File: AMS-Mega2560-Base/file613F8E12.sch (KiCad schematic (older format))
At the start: 8 parts, among them IC3 MAX31865AAP+, J2 Conn_01x02, J3 Conn_01x03, J4 Conn_01x02

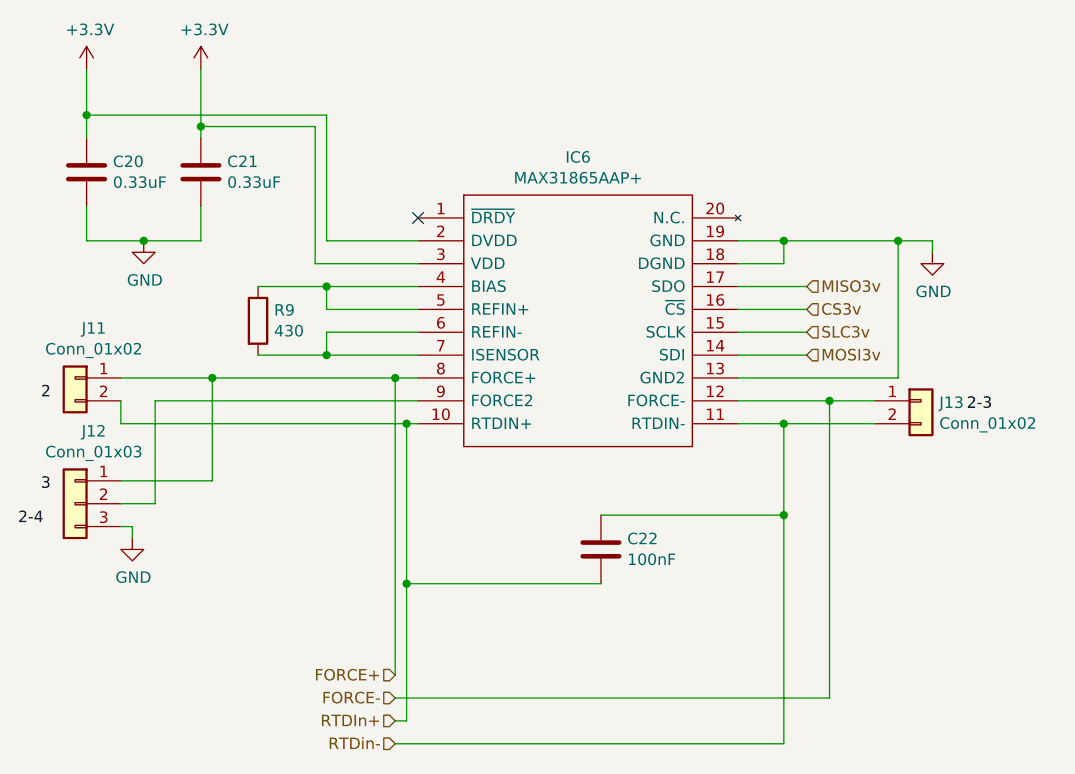
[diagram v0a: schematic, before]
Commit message: rearranging some of the hw design before i rename the repo.
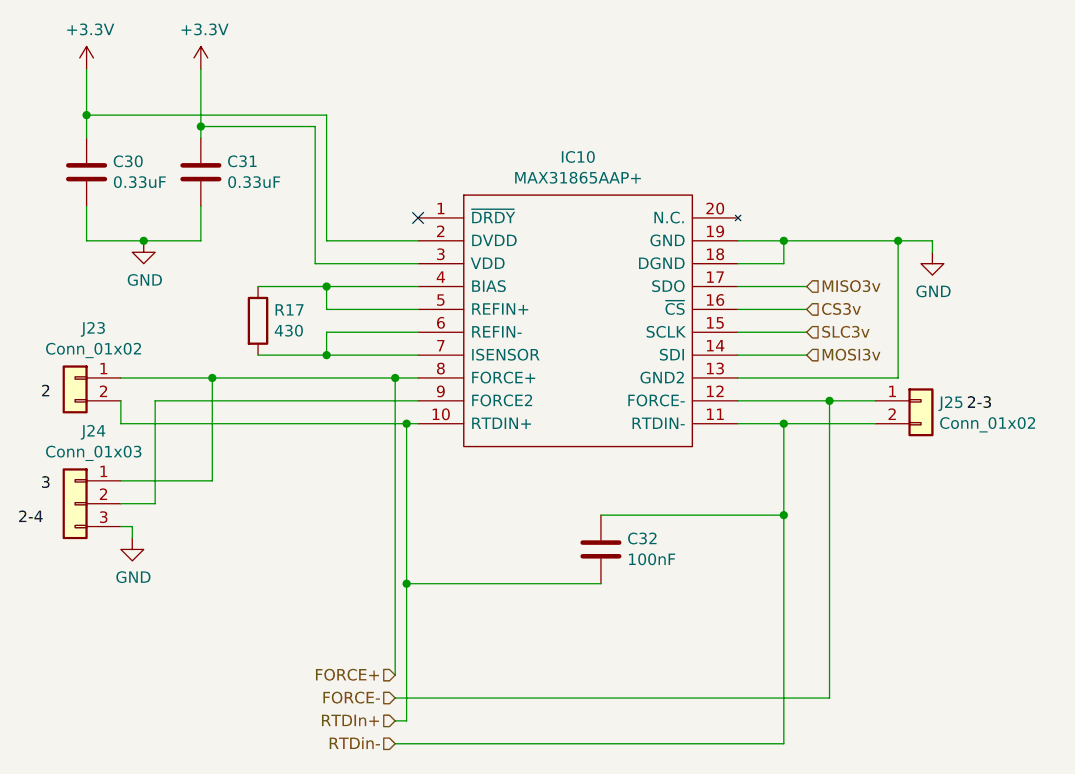
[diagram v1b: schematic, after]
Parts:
- renumbered C11 to C15, C12 to C16, C13 to C17, IC3 to IC5, J4 to J10, J2 to J8, J3 to J9, R6 to R12
